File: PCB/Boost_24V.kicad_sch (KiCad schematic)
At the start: 31 parts, among them IC1 ABXS005A4X341-SRZ, Q1 BSS138, U3 125700D00000G, U4 125700D00000G

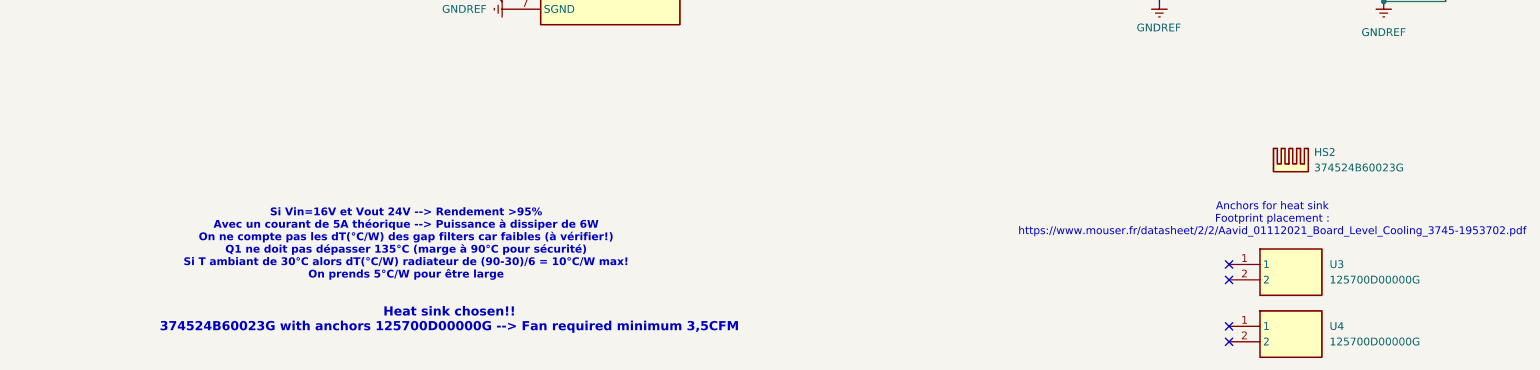
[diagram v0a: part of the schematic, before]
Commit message: ADD supplies to UC
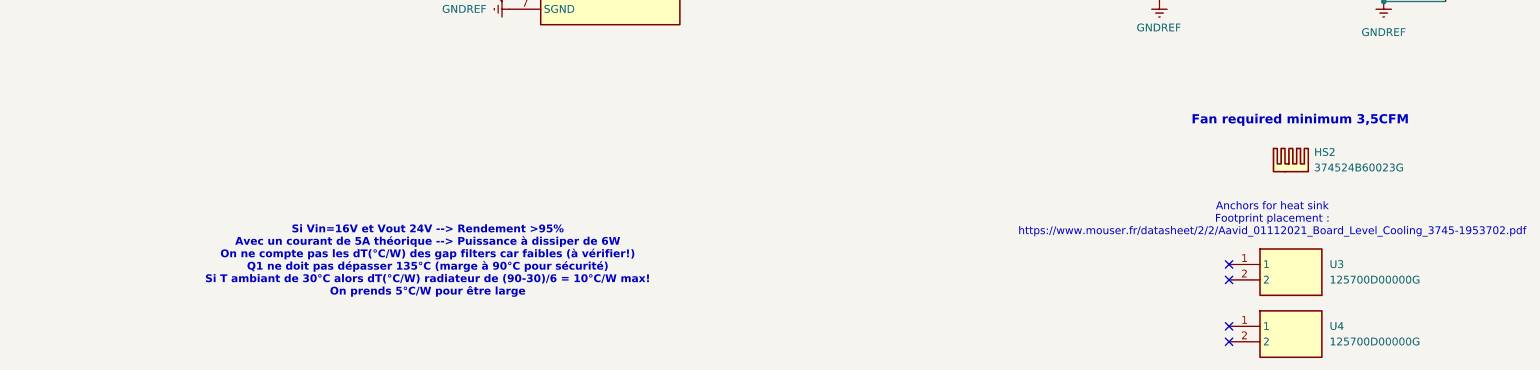
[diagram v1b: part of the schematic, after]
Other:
- note added: "Fan required minimum 3,5CFM"
- note removed: "Heat sink chosen!! 374524B60023G with anchors 125700D00000G --> Fan required minimum 3,5CFM"
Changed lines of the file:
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@@
 		)
 	)
-	(text "Heat sink chosen!!\n374524B60023G with anchors 125700D00000G --> Fan required minimum 3,5CFM"
+	(text "Fan required minimum 3,5CFM"
 		(exclude_from_sim no)
-		(at 92.964 159.004 0)
+		(at 232.664 126.238 0)
 		(effects
 			(font
@@
 	(text "Si Vin=16V et Vout 24V --> Rendement >95%\nAvec un courant de 5A théorique --> Puissance à dissiper de 6W\nOn ne compte pas les dT(°C/W) des gap filters car faibles (à vérifier!)\nQ1 ne doit pas dépasser 135°C (marge à 90°C pour sécurité)\nSi T ambiant de 30°C alors dT(°C/W) radiateur de (90-30)/6 = 10°C/W max!\nOn prends 5°C/W pour être large\n"
 		(exclude_from_sim no)
-		(at 85.852 146.558 0)
+		(at 89.408 149.352 0)
 		(effects
 			(font
